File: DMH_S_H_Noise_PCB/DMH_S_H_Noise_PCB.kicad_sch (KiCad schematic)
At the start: 0 parts

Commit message: Completed circuit
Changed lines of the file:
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@@
 	)
 	(sheet
-		(at 120.65 80.01)
-		(size 41.91 38.1)
+		(at 63.5 25.4)
+		(size 41.91 50.8)
 		(fields_autoplaced yes)
 		(stroke
@@
 		)
 		(property "Sheetname" "Core Circuit"
-			(at 120.65 79.2984 0)
+			(at 63.5 24.6884 0)
 			(effects
 				(font
@@
 		)
 		(property "Sheetfile" "Core_Circuit.kicad_sch"
-			(at 120.65 118.6946 0)
+			(at 63.5 76.7846 0)
 			(effects
 				(font
@@
 	)
 	(sheet
-		(at 17.78 17.78)
-		(size 20.32 118.11)
+		(at 17.78 63.5)
+		(size 20.32 50.8)
 		(fields_autoplaced yes)
 		(stroke
@@
 		)
 		(property "Sheetname" "Inputs and Outputs"
-			(at 17.78 17.0684 0)
+			(at 17.78 62.7884 0)
 			(effects
 				(font
@@
 		)
 		(property "Sheetfile" "Inputs_and_Outputs.kicad_sch"
-			(at 17.78 136.4746 0)
+			(at 17.78 114.8846 0)
 			(effects
 				(font

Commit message: Finished schematic
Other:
- sheet Core Circuit ports: added Blue, External Clock, Input, Internal Clock, Pink, S&H, S&H Output, Slew Input, Slew Output, White; removed none
- sheet Inputs and Outputs ports: added Blue, External Clock, Input, Internal Clock, Pink, S&H, S&H Out, Slew In, Slew Out, White; removed none
- sheet Power ports: added none; removed Bus CV, Bus Gate

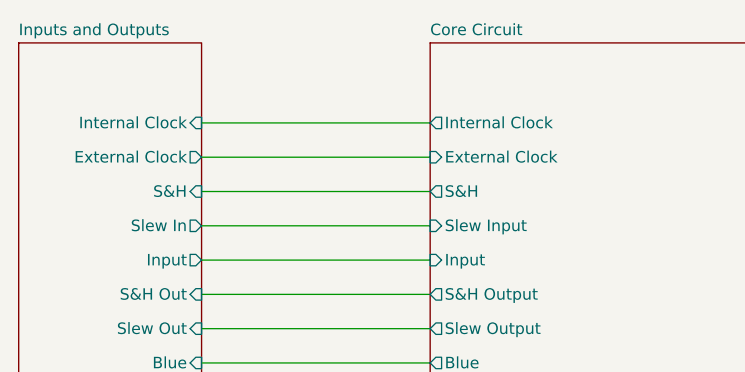
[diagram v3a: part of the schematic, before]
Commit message: Added clock output
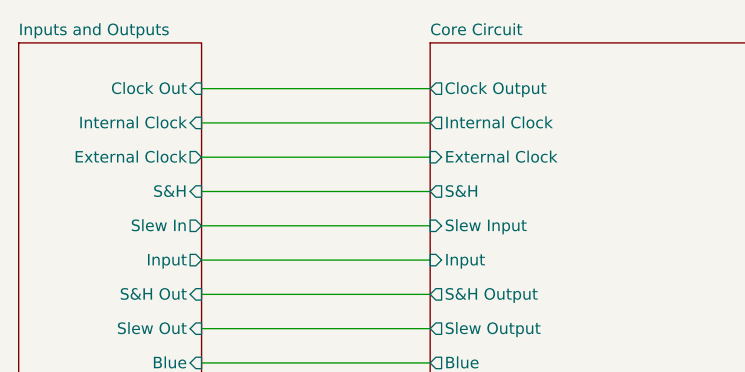
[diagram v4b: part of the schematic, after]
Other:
- sheet Core Circuit ports: added Clock Output; removed none
- sheet Inputs and Outputs ports: added Clock Out; removed none
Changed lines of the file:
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@@
+		)
+	)
+	(wire
+		(pts
+			(xy 38.1 68.58) (xy 63.5 68.58)
+		)
+		(stroke
+			(width 0)
+			(type default)
 		)
 	)
@@
 			)
 		)
+		(pin "Clock Output" output
+			(at 63.5 68.58 180)
+			(effects
+				(font
+					(size 1.27 1.27)
+				)
+				(justify left)
+			)
+		)
 		(instances
 			(project "DMH_S_H_Noise_PCB"
@@
 			(effects
 				(font
+					(size 1.27 1.27)
+				)
+				(justify right)
+			)
+		)
+		(pin "Clock Out" input
+			(at 38.1 68.58 0)
+			(effects
+				(font
